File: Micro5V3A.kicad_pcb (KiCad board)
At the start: 2 copper layers, 23.4 x 15.1 mm, 16 parts, among them J1 EnablePin, J2 5V, J3 GND, J4 VIN, J5 GND, U1 TPS563209

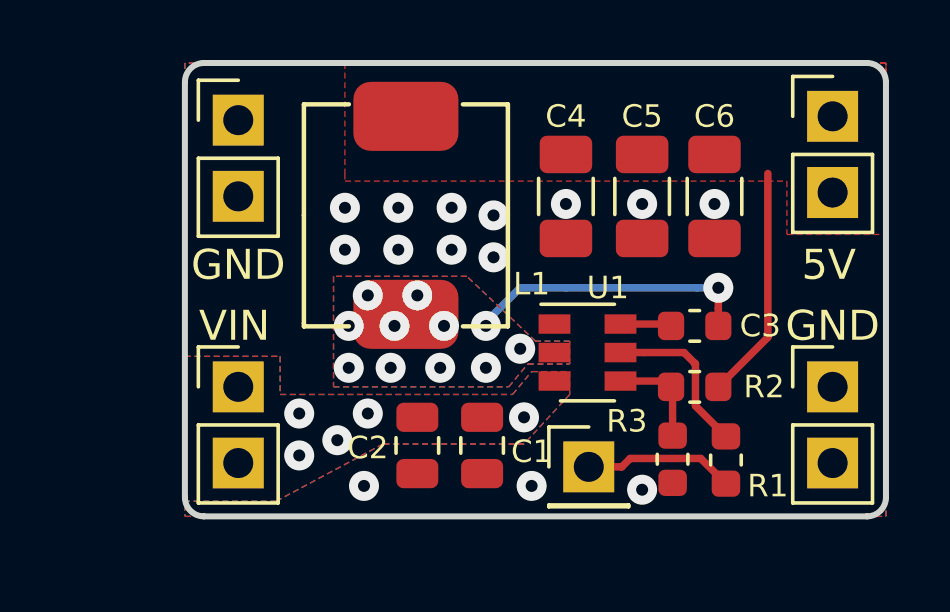
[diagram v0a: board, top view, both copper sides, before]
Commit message: Rev2 - LM7805 compatible pinout
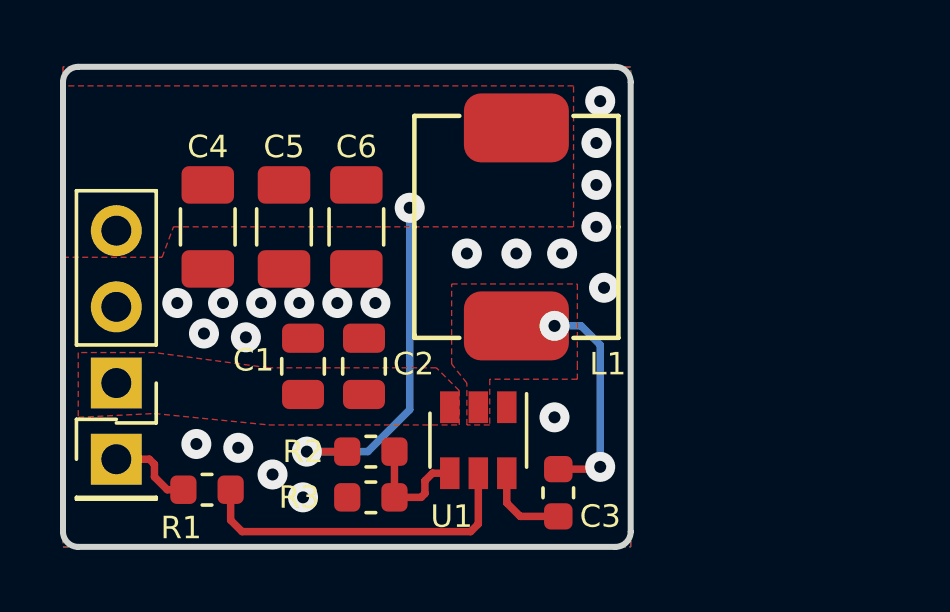
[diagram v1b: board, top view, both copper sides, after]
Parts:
- removed J3, J5: GND, Connector_PinHeader_2.54mm:PinHeader_1x02_P2.54mm_Vertical
- removed J4: VIN, Connector_PinHeader_2.54mm:PinHeader_1x02_P2.54mm_Vertical
- J2: value 5V -> Conn_01x03; footprint Connector_PinHeader_2.54mm:PinHeader_1x02_P2.54mm_Vertical -> Connector_PinHeader_2.54mm:PinHeader_1x03_P2.54mm_Vertical
- moved J2 25.5 mm to (128.9, 50.5), turned to 180 degrees
- moved R1 17.3 mm to (131.9, 54.1), turned to 180 degrees
- moved J1 15.8 mm to (128.9, 53.1)
- moved C5 12.0 mm to (134.5, 45.3)
- moved C4 12.0 mm to (132.0, 45.3)
- moved C6 12.0 mm to (136.9, 45.3)
- moved R2 11.0 mm to (137.4, 52.8), turned to 0 degrees
- moved R3 10.1 mm to (137.4, 54.4), turned to 180 degrees
- moved C3 7.18 mm to (143.6, 54.2), turned to 90 degrees
- moved C1 6.53 mm to (135.1, 50.0), turned to 90 degrees
- moved U1 4.67 mm to (141.0, 52.5), turned to 270 degrees
- moved L1 3.70 mm to (142.2, 45.3)
- moved C2 3.18 mm to (137.2, 50.0), turned to 90 degrees
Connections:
- J2 pad 1: /5V -> /VIN
- J2 pad 2: /5V -> GND
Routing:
- net Net-(R1-Pad1): track 5.54 -> 11.2 mm
- net /5V: track 7.80 -> 12.1 mm, vias 0 -> 2
- net Net-(C3-Pad2): track 9.62 -> 7.28 mm, vias 12 -> 2
- net /ENABLE: track 5.03 -> 2.90 mm
- net Net-(C3-Pad1): track 1.71 -> 2.90 mm
- net Net-(R2-Pad2): track 3.41 -> 3.95 mm
- net GND: vias 14 -> 21
- net /VIN: vias 5 -> 0
- removed copper zone on B.Cu, net /VIN
- removed copper zone on B.Cu, net Net-(C3-Pad2)
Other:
- board size 23.4 x 15.1 mm -> 18.9 x 16 mm
- board text added: "5V, 3A, 7-17 VIN O. Pecák, April 2019"
- board text added: "Enable"
- board text removed: "5V 3A Power module VIN 7V - 17V"
- board text removed: "GND"
- board text removed: "O. Pecák April 2019"
